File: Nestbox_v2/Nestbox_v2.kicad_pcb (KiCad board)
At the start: 2 copper layers, 91 parts, among them CON301 Micro_SD_Card, J201 CONN_01X02, J401 CONN_01X04, J402 CONN_01X04, J403 CONN_01X04, J601 CONN_01X04, J701 CONN_01X05, P301 RX/TX, P302 TST/RST, Q701 Q_NMOS_DGS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

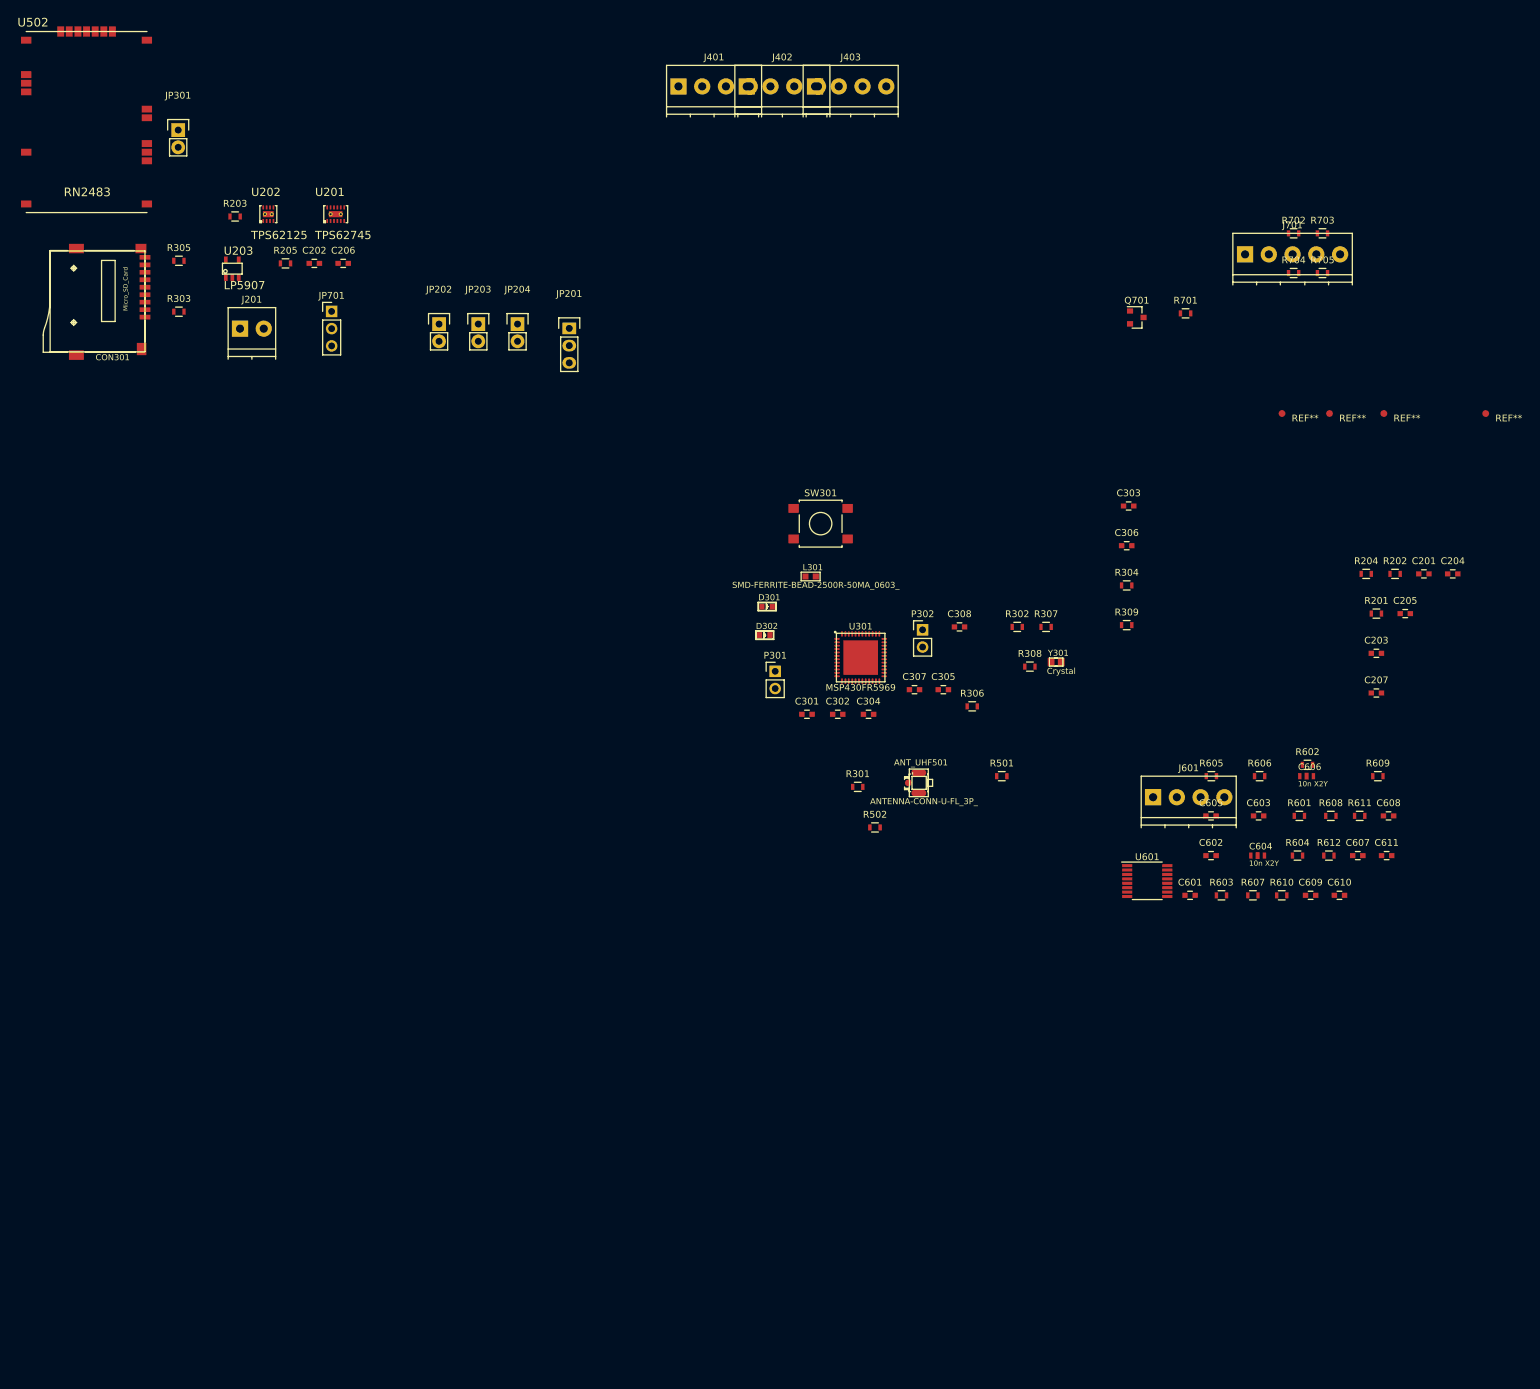
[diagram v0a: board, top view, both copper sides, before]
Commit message: correct size of the PCB drawn with connector arrangement done as well
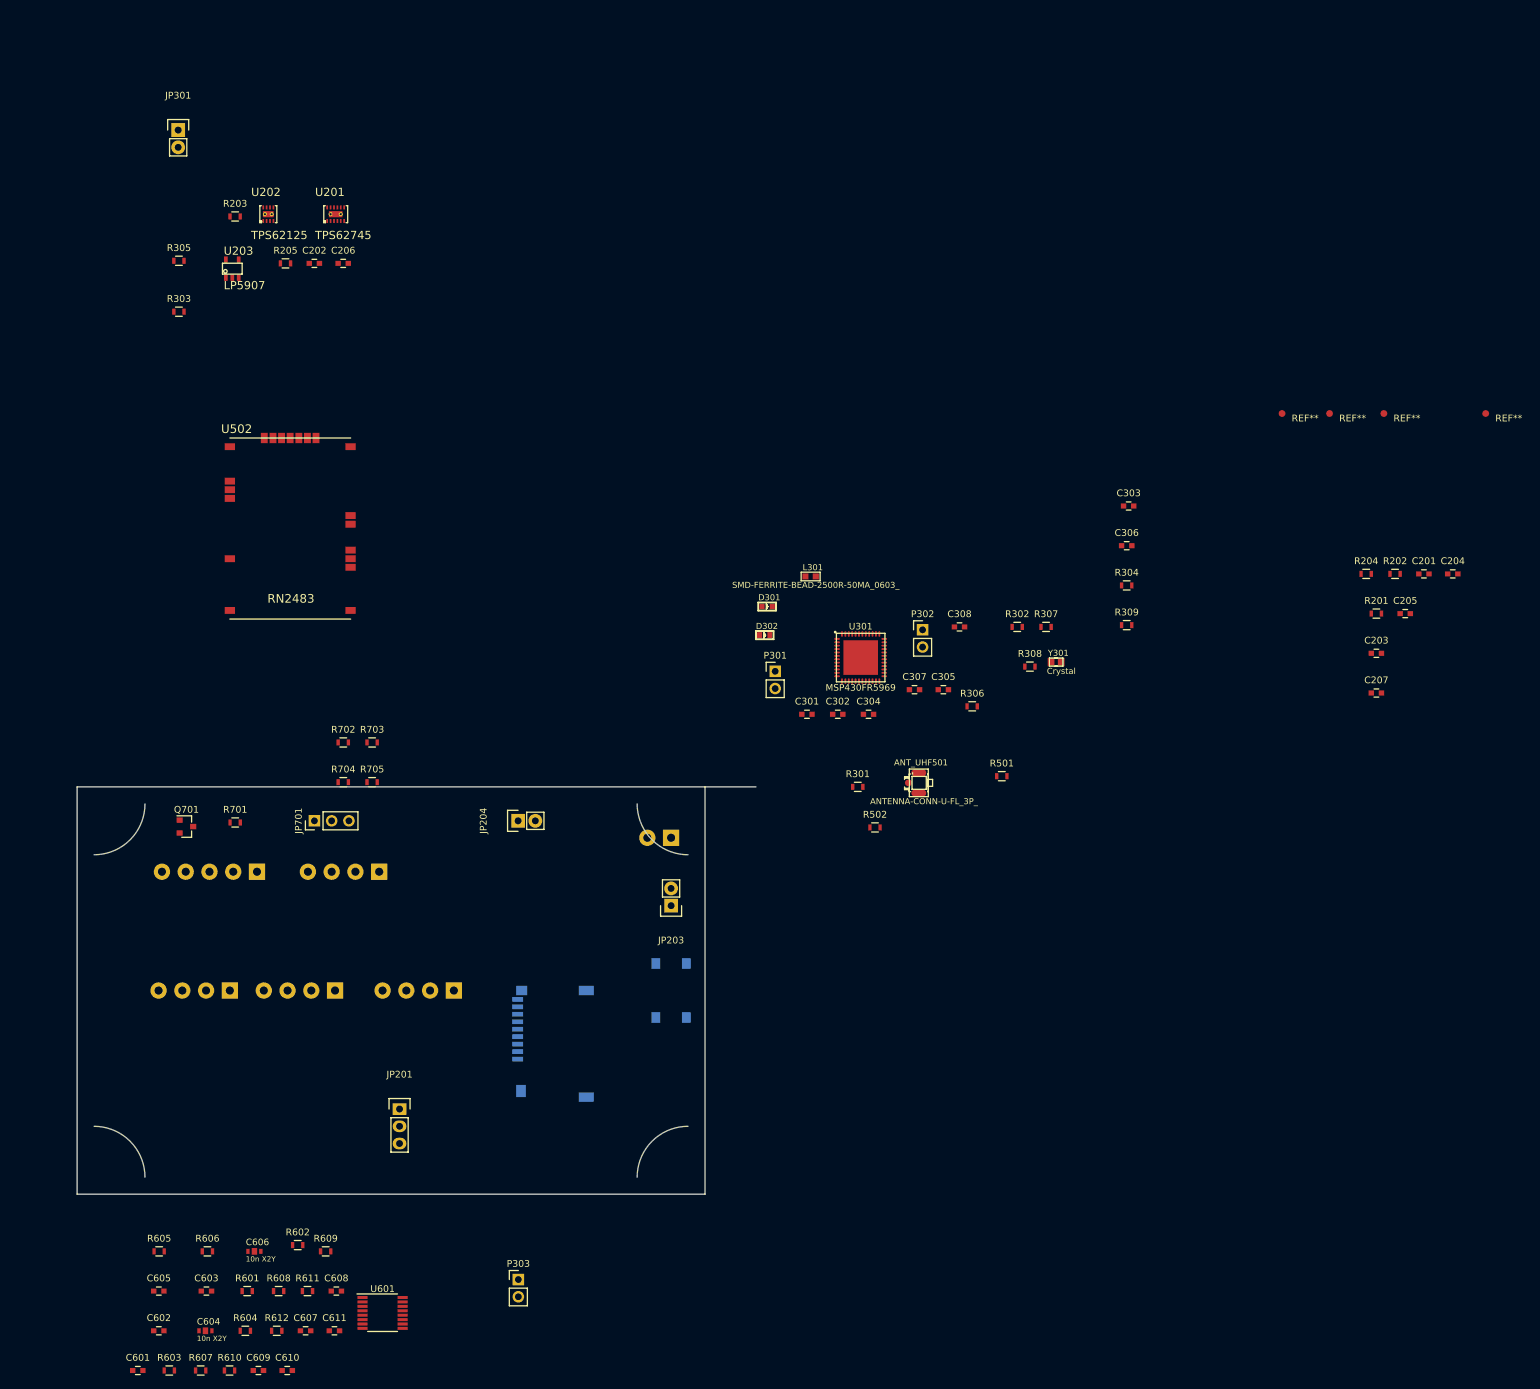
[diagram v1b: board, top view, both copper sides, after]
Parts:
- removed JP202: Jumper, Pin_Headers:Pin_Header_Straight_1x02
- added P303: DEBUG_3V3, Socket_Strips:Socket_Strip_Straight_1x02_Pitch2.54mm, F.Cu at (90.0, 200.1)
- C604, C606: footprint murata-filter:NFM21P -> murata-filter:NFM18PS
- CON301, SW301: moved to B.Cu
- J201: value CONN_01X02 -> BATT_CONN_01X02; moved to B.Cu
- J401: value CONN_01X04 -> LB_DETECT_CONN_01X04; moved to B.Cu
- J402: value CONN_01X04 -> PIR_CONN_01X04; moved to B.Cu
- J403: value CONN_01X04 -> LB_LED_CONN_01X04; moved to B.Cu
- J601: value CONN_01X04 -> LOAD_CELL_CONN_01X04; moved to B.Cu
- J701: value CONN_01X05 -> RFID_CONN_01X05; moved to B.Cu
- JP201: value Jumper_SELECT_Dual -> VAA_Jumper_SELECT_Dual
- JP203: value Jumper -> Jumper_3V3
- JP204: value Jumper -> Jumper_5V
- JP701: value Jumper_SELECT_Dual -> V_RFID_Jumper_SELECT_Dual
- moved J701 171.6 mm to (51.5, 140.0), turned to 180 degrees
- moved C601 170.1 mm to (33.9, 213.5)
- moved C602 170.1 mm to (37.0, 207.6)
- moved C603 170.1 mm to (44.0, 201.8)
- moved C604 170.1 mm to (43.9, 207.6)
- moved C605 170.1 mm to (37.0, 201.8)
- moved C606 170.1 mm to (51.1, 195.9)
- moved C607 170.1 mm to (58.7, 207.6)
- moved C608 170.1 mm to (63.2, 201.8)
- moved C609 170.1 mm to (51.7, 213.5)
- moved C610 170.1 mm to (56.0, 213.5)
- moved C611 170.1 mm to (62.9, 207.6)
- moved R601 170.1 mm to (50.1, 201.8)
- moved R603 170.1 mm to (38.6, 213.5)
- moved R604 170.1 mm to (49.8, 207.6)
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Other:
- board outline added: 100 x 60 mm

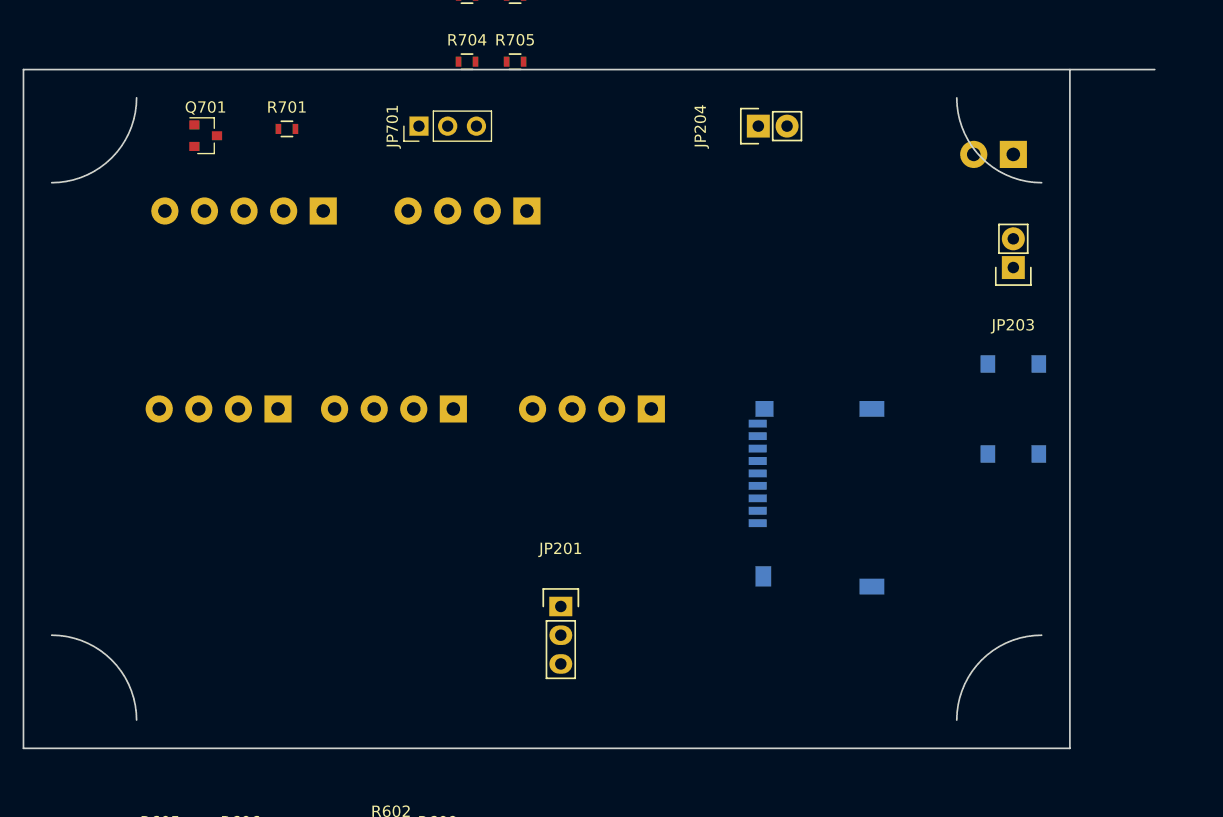
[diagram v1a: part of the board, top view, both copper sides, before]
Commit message: final board size, mounting holes
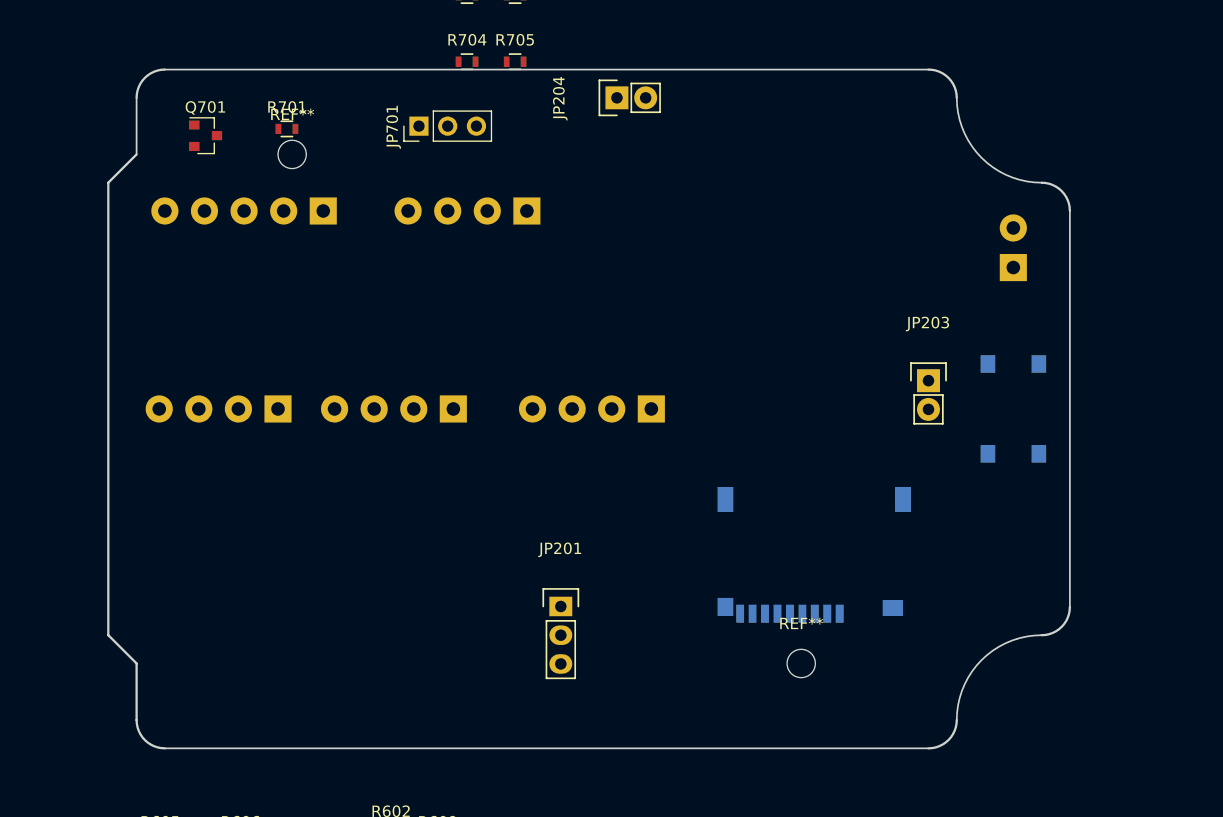
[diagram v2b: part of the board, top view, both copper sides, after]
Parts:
- added REF**: MountingHole_2.5mm, Mounting_Holes:MountingHole_2.5mm, F.Cu at (93.8, 180.0)
- added REF**: MountingHole_2.5mm, Mounting_Holes:MountingHole_2.5mm, F.Cu at (48.8, 135.0)
- moved JP204 12.7 mm to (77.5, 130.0)
- moved JP203 12.5 mm to (105.0, 155.0), turned to 0 degrees
- moved CON301 11.4 mm to (94.9, 175.6), turned to 90 degrees
- moved J201 10.0 mm to (112.5, 145.0), turned to 90 degrees
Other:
- board size 100 x 60 mm -> 85 x 60 mm
